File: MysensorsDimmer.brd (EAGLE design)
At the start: 64.7 x 64.7 mm, 56 parts, among them IC1 7805DT, IC2 AT25DF512C-SSHN-B, IC3 ATSHA204A, IC4 DS1820, J1 22-27-2021-02, J2 22-27-2021-02, J3 22-27-2021-02, J4 22-27-2021-02, J5 22-27-2021-02, Q1 IRF530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

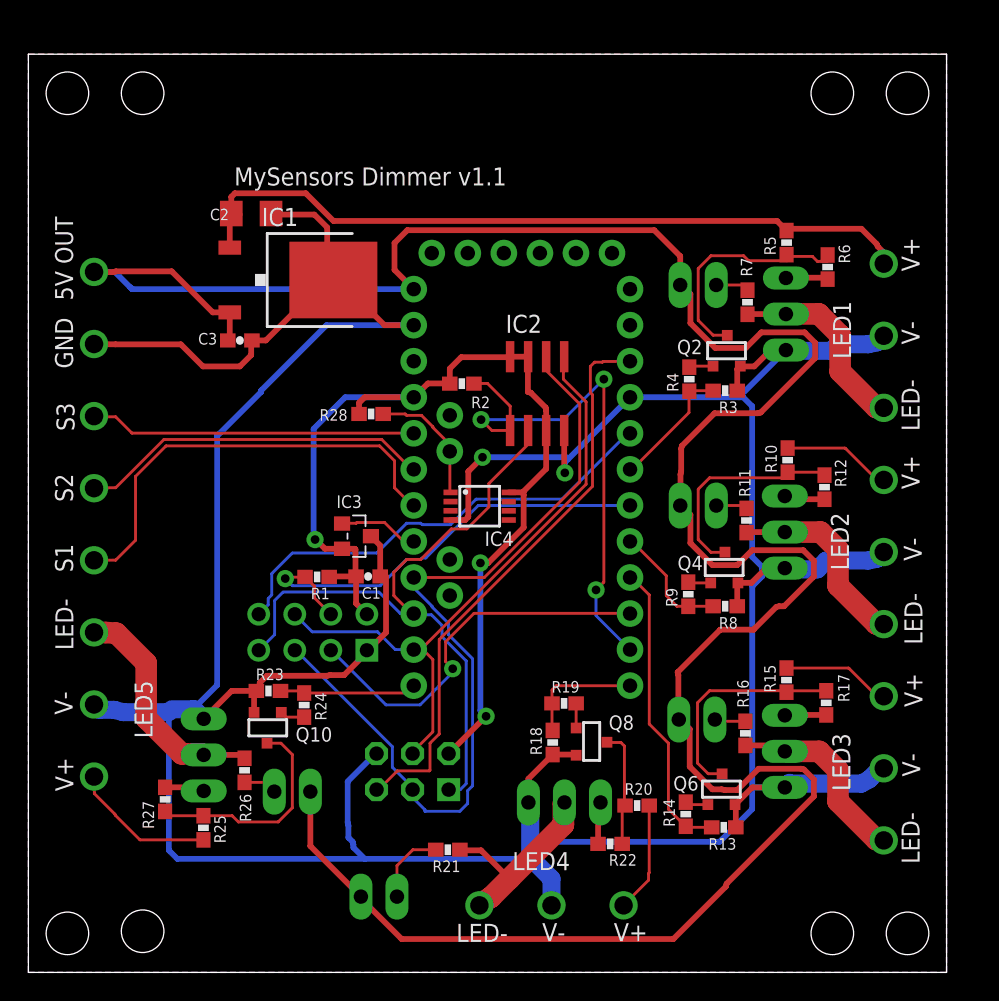
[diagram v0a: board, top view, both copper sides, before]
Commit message: add i2c connection for apds 9930
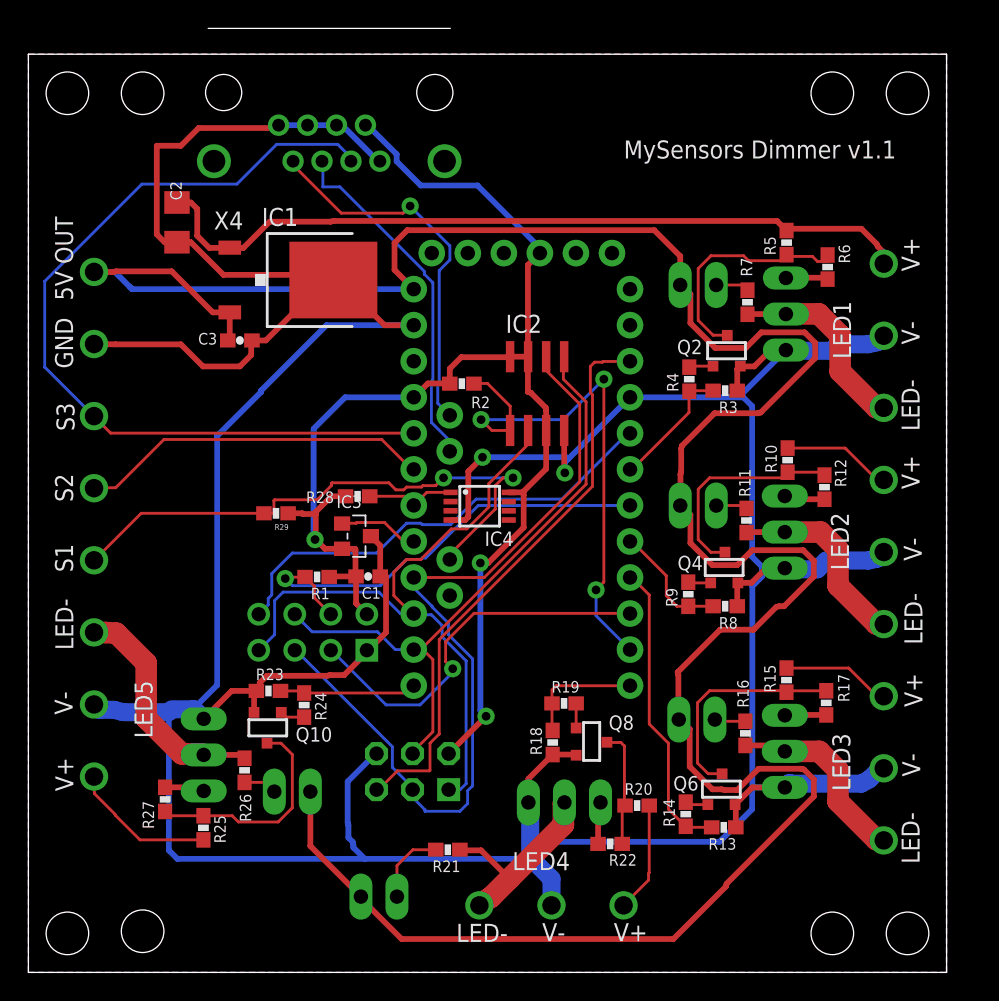
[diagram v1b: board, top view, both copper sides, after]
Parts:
- added R29: 10k, SparkFun-Passives:0603-RES
- added X4: GLX-S-88M, con-kycon:GLX-S-88M
- moved R28 5.88 mm to (23.2, 33.5)
- moved C2 5.26 mm to (10.5, 52.9), turned to 90 degrees
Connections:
- new net A6: ARDUINO1.A6
- new net A7: ARDUINO1.A7, R29.2, X2.4
- net A1: now also IC4.1, R28.1; no longer X2.4
- net A3: now also X4.6
- net A4: now also X4.4; no longer IC4.1, R28.1
- net A5: now also X4.2
- net GND: now also X4.1, X4.3, X4.5, X4.8
- net VCC: now also ARDUINO1.VCC', R29.1, X4.7
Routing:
- net A7: track 0.00 -> 41.0 mm, vias 0 -> 2
- net A3: track 23.0 -> 60.2 mm
- net GND: track 291.2 -> 320.2 mm
- net A5: track 0.00 -> 26.7 mm, vias 0 -> 1
- net VCC: track 73.6 -> 99.5 mm
- net A1: track 31.4 -> 6.34 mm
- net A4: track 9.02 -> 25.0 mm
- net 12V: track 53.1 -> 54.9 mm
